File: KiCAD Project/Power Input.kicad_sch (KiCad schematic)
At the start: 11 parts, among them J1 S2B-XH-A-1, Q1 BUK6D120-60PX

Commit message: v1.0.0 RC2
Build candidate 2
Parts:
- J1: Manufacturer_Part_Number B2B-XH-A(LF)(SN) -> S2B-XH-A-1; Mouser Part Number (none) -> 306-S2BXHA1LFSN; Mouser Price/Stock (none) -> https://www.mouser.com/ProductDetail/JST-Commercial/S2B-XH-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
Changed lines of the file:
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@@
 			)
 		)
-		(property "Mouser Part Number" ""
+		(property "Mouser Part Number" "306-S2BXHA1LFSN"
 			(at 45.72 53.34 0)
 			(effects
@@
 			)
 		)
-		(property "Manufacturer_Part_Number" "B2B-XH-A(LF)(SN)"
+		(property "Manufacturer_Part_Number" "S2B-XH-A-1"
 			(at 45.72 74.93 0)
 			(effects
@@
 			)
 		)
+		(property "Mouser Price/Stock" "https://www.mouser.com/ProductDetail/JST-Commercial/S2B-XH-A-1LFSN?qs=QpmGXVUTftHhNeC%252BPQWeTw%3D%3D"
+			(at 45.72 53.34 0)
+			(effects
+				(font
+					(size 1.27 1.27)
+				)
+			)
+		)

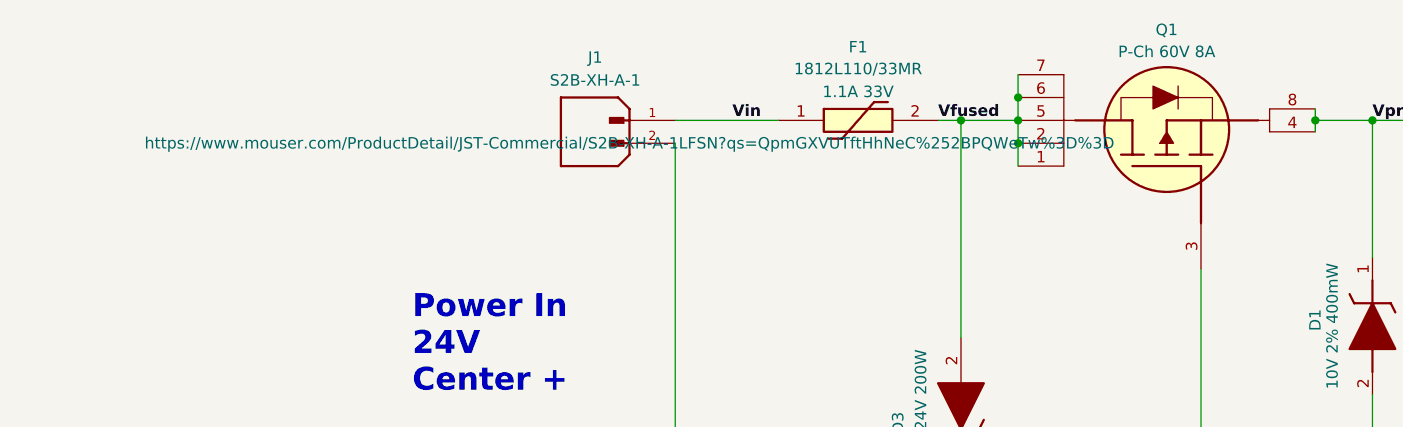
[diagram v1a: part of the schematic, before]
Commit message: v1.0.0 RC3
Minor change to upstream USB port to connect Vbus to ESD protection vice on-board 5V.
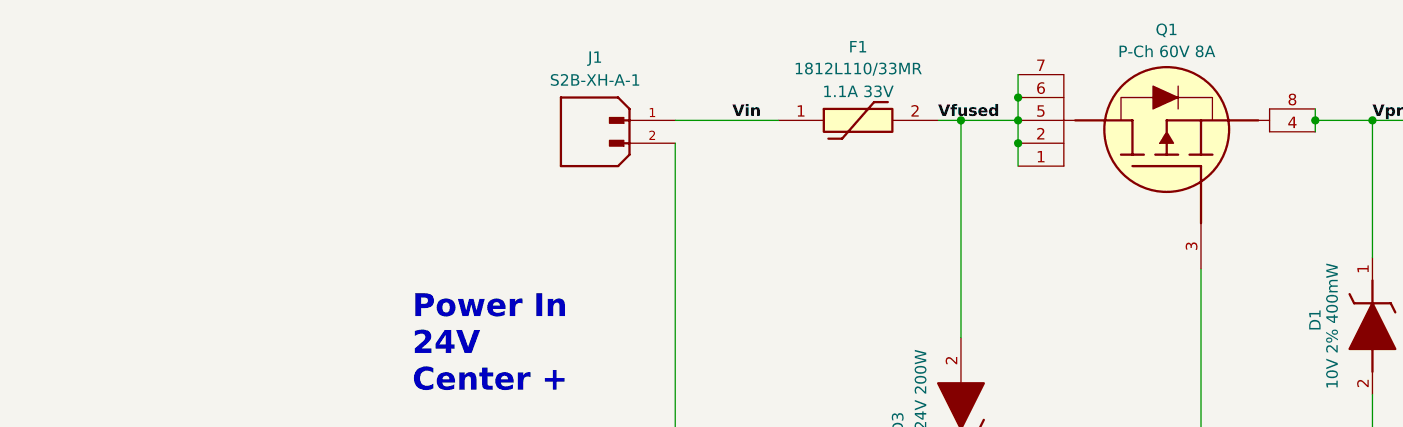
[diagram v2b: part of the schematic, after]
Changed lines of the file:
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@@
 		(title "1026 RPi Power Hat")
 		(date "2025-04-11")
-		(rev "1")
+		(rev "1.0.0 RC3")
 		(company "Dan Wilson")
 		(comment 1 "Copyright © 2025 Dan Wilson")
@@
 					(size 1.27 1.27)
 				)
-			)
-		)
+				(hide yes)
+			)
+		)

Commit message: v1.0.0A
Moved all symbols, footprints, and 3D models to local project-specific libraries in /KiCAD Project/Libraries.
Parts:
- C1, C2: footprint DW_Passives:[C] Kemet Tantalum Polymer T521X -> 1026-3D:[C] Kemet Tantalum Polymer T521X; symbol DW_Passives:[C] Kemet Tantalum Polymer T521X336M050ATE050 -> 1026-3D:[C] Kemet Tantalum Polymer T521X336M050ATE050
- D1: footprint DW_Semiconductors:[D] Nexperia Zener PDZ10B,115 10V -> 1026-3D:[D] Nexperia Zener PDZ10B,115 10V; symbol DW_Semiconductors:[D] Nexperia Zener PDZ10B,115 10V -> 1026-3D:[D] Nexperia Zener PDZ10B,115 10V
- D2: footprint DW_Optoelectronics:[D] Wurth Elektronik 150040GS73220 -> 1026-3D:[D] Wurth Elektronik 150040GS73220; symbol DW_Optoelectronics:[D] Wurth Elektronik 150040GS73220 -> 1026-3D:[D] Wurth Elektronik 150040GS73220
- D3: footprint DW_CircuitProtection:[D] Littelfuse SMF24CA 24V 200W -> 1026-3D:[D] Littelfuse SMF24CA 24V 200W; symbol DW_CircuitProtection:[D] Littelfuse SMF24CA 24V 200W -> 1026-3D:[D] Littelfuse SMF24CA 24V 200W
- F1: footprint DW_CircuitProtection:[F] Littelfuse PPTC 1812L010DR -> 1026-3D:[F] Littelfuse PPTC 1812L010DR; symbol DW_CircuitProtection:[F] Littelfuse 1812L110/33MR PPTC 1.1A -> 1026-3D:[F] Littelfuse 1812L110/33MR PPTC 1.1A
- J1: footprint DW_Connectors:[J] JST S2B-XH-A-1 -> 1026-3D:[J] JST S2B-XH-A-1; symbol DW_Connectors:[J] JST S2B-XH-A-1 -> 1026-3D:[J] JST S2B-XH-A-1
- L1: footprint DW_Passives:[L] Coilcraft Inductor LPS4040 -> 1026-3D:[L] Coilcraft Inductor LPS4040; symbol DW_Passives:[L] Coilcraft Inductor LPS4040 22uH 210mohm -> 1026-3D:[L] Coilcraft Inductor LPS4040 22uH 210mohm
- Q1: footprint DW_Semiconductors:[Q] Nexperia BUK6D120-60PX P-Ch 60V 8A -> 1026-3D:[Q] Nexperia BUK6D120-60PX P-Ch 60V 8A; symbol DW_Semiconductors:[Q] Nexperia BUK6D120-60PX P-Ch 60V 8A -> 1026-3D:[Q] Nexperia BUK6D120-60PX P-Ch 60V 8A
- R1, R2: footprint Resistor_SMD:R_0402_1005Metric -> 1026-3D:R_0402_1005Metric; symbol Device:R_US -> 1026-3D:R_US
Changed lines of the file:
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@@
 	)
 	(symbol
-		(lib_id "DW_CircuitProtection:[F] Littelfuse 1812L110/33MR PPTC 1.1A")
+		(lib_id "1026-3D:[F] Littelfuse 1812L110/33MR PPTC 1.1A")
 		(at 62.23 50.8 0)
 		(unit 1)
@@
 			)
 		)
-		(property "Footprint" "DW_CircuitProtection:[F] Littelfuse PPTC 1812L010DR"
+		(property "Footprint" "1026-3D:[F] Littelfuse PPTC 1812L010DR"
 			(at 76.2 146.99 0)
 			(effects
@@
 	)
 	(symbol
-		(lib_id "power:PWR_FLAG")
+		(lib_id "1026-3D:PWR_FLAG")
 		(at 184.15 129.54 180)
 		(unit 1)
@@
 	)
 	(symbol
-		(lib_id "DW_CircuitProtection:[D] Littelfuse SMF24CA 24V 200W")
+		(lib_id "1026-3D:[D] Littelfuse SMF24CA 24V 200W")
 		(at 82.55 95.25 90)
 		(unit 1)
@@
 			)
 		)
-		(property "Footprint" "DW_CircuitProtection:[D] Littelfuse SMF24CA 24V 200W"
+		(property "Footprint" "1026-3D:[D] Littelfuse SMF24CA 24V 200W"
 			(at 176.2 82.55 0)
 			(effects
@@
 	)
 	(symbol
-		(lib_id "DW_Semiconductors:[D] Nexperia Zener PDZ10B,115 10V")
+		(lib_id "1026-3D:[D] Nexperia Zener PDZ10B,115 10V")
 		(at 128.27 66.04 270)
 		(unit 1)
@@
 			)
 		)
-		(property "Footprint" "DW_Semiconductors:[D] Nexperia Zener PDZ10B,115 10V"
+		(property "Footprint" "1026-3D:[D] Nexperia Zener PDZ10B,115 10V"
 			(at 34.62 76.2 0)
 			(effects
@@
 	)
 	(symbol
-		(lib_id "DW_Passives:[L] Coilcraft Inductor LPS4040 22uH 210mohm")
+		(lib_id "1026-3D:[L] Coilcraft Inductor LPS4040 22uH 210mohm")
 		(at 142.24 50.8 0)
 		(unit 1)
@@
 			)
 		)
-		(property "Footprint" "DW_Passives:[L] Coilcraft Inductor LPS4040"
+		(property "Footprint" "1026-3D:[L] Coilcraft Inductor LPS4040"
 			(at 158.75 146.99 0)
 			(effects
@@
 	)
 	(symbol
-		(lib_id "Device:R_US")
+		(lib_id "1026-3D:R_US")
 		(at 184.15 69.85 0)
 		(unit 1)
@@
 			)
 		)
-		(property "Footprint" "Resistor_SMD:R_0402_1005Metric"
+		(property "Footprint" "1026-3D:R_0402_1005Metric"
 			(at 185.166 70.104 90)
 			(effects
@@
 	)
 	(symbol
-		(lib_id "DW_Semiconductors:[Q] Nexperia BUK6D120-60PX P-Ch 60V 8A")
+		(lib_id "1026-3D:[Q] Nexperia BUK6D120-60PX P-Ch 60V 8A")
 		(at 105.41 68.58 90)
 		(unit 1)
@@
 			)
 		)
-		(property "Footprint" "DW_Semiconductors:[Q] Nexperia BUK6D120-60PX P-Ch 60V 8A"
+		(property "Footprint" "1026-3D:[Q] Nexperia BUK6D120-60PX P-Ch 60V 8A"
 			(at 200.33 46.99 0)
 			(effects
@@
 	)
 	(symbol
-		(lib_id "DW_Passives:[C] Kemet Tantalum Polymer T521X336M050ATE050")
+		(lib_id "1026-3D:[C] Kemet Tantalum Polymer T521X336M050ATE050")
 		(at 139.7 85.09 270)
 		(unit 1)
@@
 			)
 		)
-		(property "Footprint" "DW_Passives:[C] Kemet Tantalum Polymer T521X"
+		(property "Footprint" "1026-3D:[C] Kemet Tantalum Polymer T521X"
 			(at 43.51 93.98 0)
 			(effects
@@
 	)
 	(symbol
-		(lib_id "DW_Optoelectronics:[D] Wurth Elektronik 150040GS73220")
+		(lib_id "1026-3D:[D] Wurth Elektronik 150040GS73220")
 		(at 184.15 120.65 90)
 		(unit 1)
@@
 			)
 		)
-		(property "Footprint" "DW_Optoelectronics:[D] Wurth Elektronik 150040GS73220"
+		(property "Footprint" "1026-3D:[D] Wurth Elektronik 150040GS73220"
 			(at 277.8 107.95 0)
 			(effects
@@
 	)
 	(symbol
-		(lib_id "DW_Passives:[C] Kemet Tantalum Polymer T521X336M050ATE050")
+		(lib_id "1026-3D:[C] Kemet Tantalum Polymer T521X336M050ATE050")
 		(at 165.1 85.09 270)
 		(unit 1)
@@
 			)
 		)
-		(property "Footprint" "DW_Passives:[C] Kemet Tantalum Polymer T521X"
+		(property "Footprint" "1026-3D:[C] Kemet Tantalum Polymer T521X"
 			(at 68.91 93.98 0)
 			(effects
@@
 	)
 	(symbol
-		(lib_id "power:GND")
+		(lib_id "1026-3D:GND")
 		(at 165.1 129.54 0)
 		(unit 1)
@@
 	)
 	(symbol
-		(lib_id "DW_Connectors:[J] JST S2B-XH-A-1")
+		(lib_id "1026-3D:[J] JST S2B-XH-A-1")
 		(at 45.72 53.34 0)
 		(mirror y)
@@
 			)
 		)
-		(property "Footprint" "DW_Connectors:[J] JST S2B-XH-A-1"
+		(property "Footprint" "1026-3D:[J] JST S2B-XH-A-1"
 			(at 45.72 64.77 0)
 			(effects
@@
 	)
 	(symbol
-		(lib_id "power:PWR_FLAG")
+		(lib_id "1026-3D:PWR_FLAG")
 		(at 210.82 50.8 180)
 		(unit 1)
@@
 	)
 	(symbol
-		(lib_id "Device:R_US")
+		(lib_id "1026-3D:R_US")
 		(at 109.22 116.84 0)
 		(unit 1)
@@
 			)
 		)
-		(property "Footprint" "Resistor_SMD:R_0402_1005Metric"
+		(property "Footprint" "1026-3D:R_0402_1005Metric"
 			(at 110.236 117.094 90)
 			(effects
